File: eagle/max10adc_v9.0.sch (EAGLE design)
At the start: 206 parts, among them IC1 MAX19506, IC2 MAX19506, J1 MOLEX_BNC_73100-0105, J2 MOLEX_BNC_73100-0105, J3 MOLEX_BNC_73100-0105, J4 MOLEX_BNC_73100-0105, K1 AQY21SOP, K2 AQY21SOP, K3 AQY21SOP, K4 AQY21SOP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

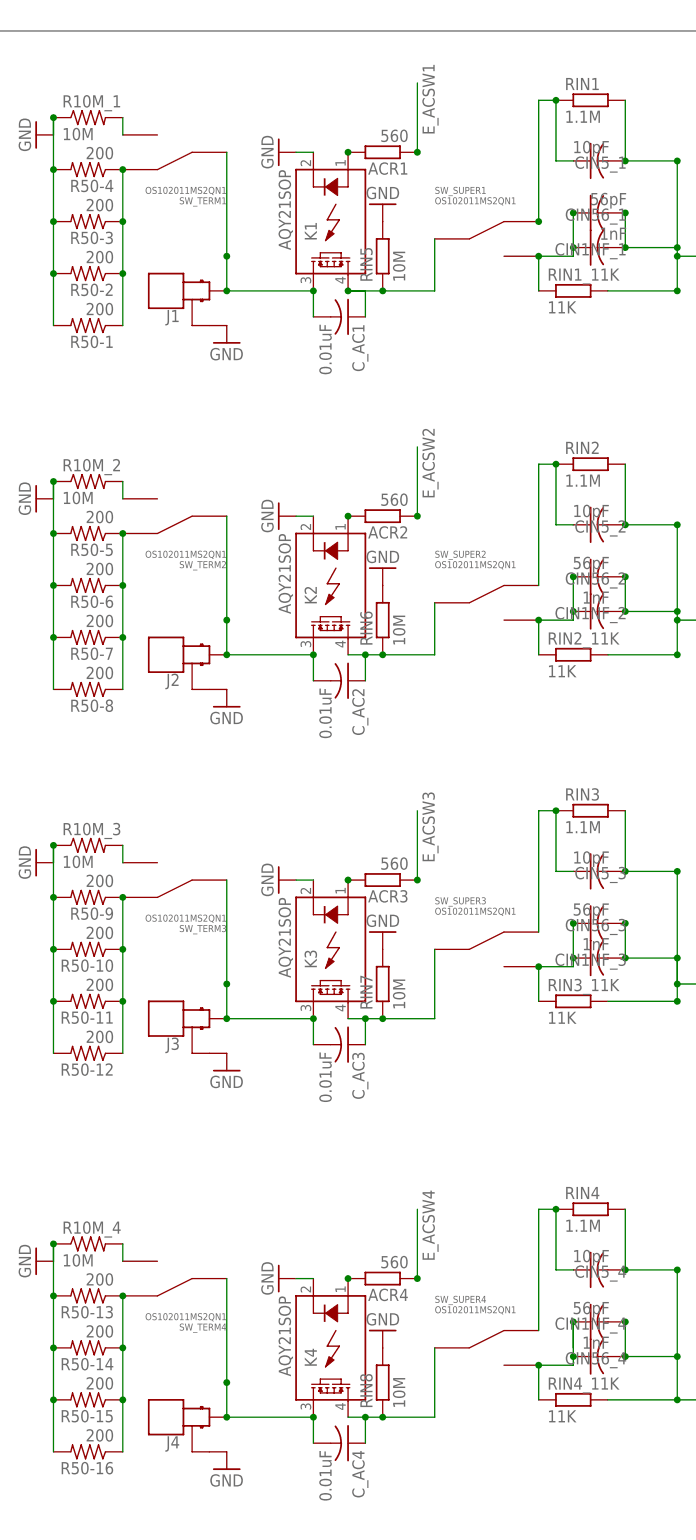
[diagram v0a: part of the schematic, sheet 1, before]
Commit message: updates for board 9.0 with dpdt switches
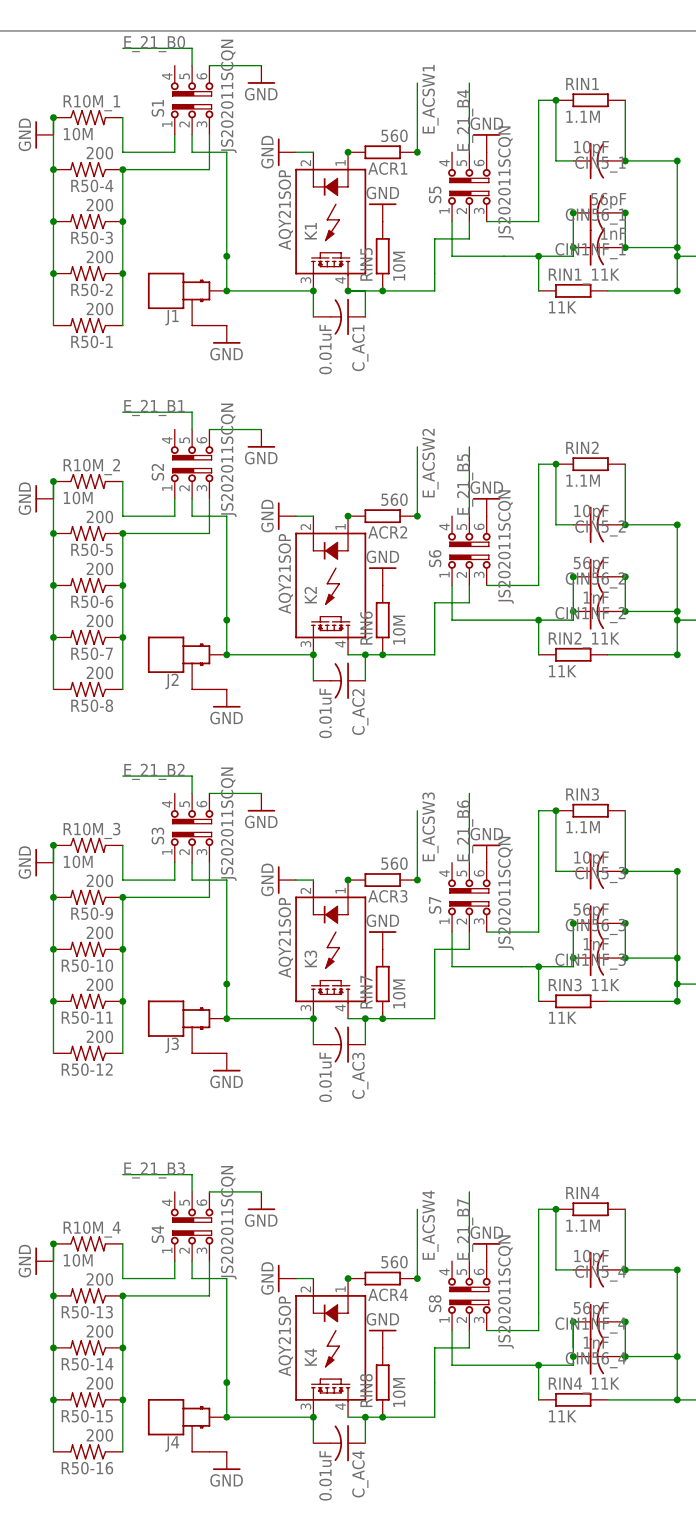
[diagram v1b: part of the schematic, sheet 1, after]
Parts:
- removed LED5, LED6, LED7, LED8: MF-LED-0805-RED, led:LEDSML0805
- removed RLED5, RLED6, RLED7, RLED8: 560, resistor:R-EU_R0805
- removed SW_5V, SW_SUPER1, SW_SUPER2, SW_SUPER3, SW_SUPER4, SW_TERM1, SW_TERM2, SW_TERM3, SW_TERM4: OS102011MS2QN1, PP_Electromechanical:SPDT_0S102011MS2QS1
- added S1, S2, S3, S4, S5, S6, S7, S8, S9: JS202011SCQN, switch-ck:JS202011SCQN
- renumbered IOEXPAND_0X24_TOP to IOEXPAND_0X21_TOP
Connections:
- removed net DCLKA1: IC1.DCLKA
- removed net DCLKA2: IC2.DCLKA
- removed net DCLKB1: IC1.DCLKB
- removed net DCLKB2: IC2.DCLKB
- removed net DORA1: IC1.DORA
- removed net DORA2: IC2.DORA
- removed net DORB1: IC1.DORB
- removed net DORB2: IC2.DORB
- removed net E_24_B0: IOEXPAND_0X21_TOP.GPB0, PIN_ANALOG_IOEXP.1
- removed net E_24_B1: IOEXPAND_0X21_TOP.GPB1, PIN_ANALOG_IOEXP.3
- removed net E_24_B2: IOEXPAND_0X21_TOP.GPB2, PIN_ANALOG_IOEXP.5
- removed net E_24_B3: IOEXPAND_0X21_TOP.GPB3, PIN_ANALOG_IOEXP.7
- removed net E_24_B4: IOEXPAND_0X21_TOP.GPB4, PIN_ANALOG_IOEXP.9
- removed net E_24_B5: IOEXPAND_0X21_TOP.GPB5, PIN_ANALOG_IOEXP.11
- removed net E_24_B6: IOEXPAND_0X21_TOP.GPB6, PIN_ANALOG_IOEXP.13
- removed net E_24_B7: IOEXPAND_0X21_TOP.GPB7, PIN_ANALOG_IOEXP.15
- removed net LED5: IOEXPAND_0X21_TOP.GPA4, LED5.A
- removed net LED6: IOEXPAND_0X21_TOP.GPA5, LED6.A
- removed net LED7: IOEXPAND_0X21_TOP.GPA6, LED7.A
- removed net LED8: IOEXPAND_0X21_TOP.GPA7, LED8.A
- removed net N$16: LED6.C, RLED6.1
- removed net N$17: LED5.C, RLED5.1
- removed net N$38: CIN1NF_2.1, CIN56_2.1, RIN2_11K.1, SW_SUPER2.2
- removed net N$40: CIN1NF_3.1, CIN56_3.1, RIN3_11K.1, SW_SUPER3.2
- removed net N$42: CIN5_3.1, RIN3.1, SW_SUPER3.1
- removed net N$52: CIN5_4.1, RIN4.1, SW_SUPER4.1
- removed net N$53: CIN1NF_4.1, CIN56_4.1, RIN4_11K.1, SW_SUPER4.2
- removed net N$61: CIN5_2.1, RIN2.1, SW_SUPER2.1
- new net E_21_B0: IOEXPAND_0X21_TOP.GPB0, S1.5
- new net E_21_B1: IOEXPAND_0X21_TOP.GPB1, S2.5
- new net E_21_B2: IOEXPAND_0X21_TOP.GPB2, S3.5
- new net E_21_B3: IOEXPAND_0X21_TOP.GPB3, S4.5
- new net E_21_B4: IOEXPAND_0X21_TOP.GPB4, S5.5
- new net E_21_B5: IOEXPAND_0X21_TOP.GPB5, S6.5
- new net E_21_B6: IOEXPAND_0X21_TOP.GPB6, S7.5
- new net E_21_B7: IOEXPAND_0X21_TOP.GPB7, S8.5
- new net E_IO_1: IOEXPAND_0X21_TOP.GPA4, PIN_ANALOG_IOEXP.1
- new net E_IO_2: IOEXPAND_0X21_TOP.GPA5, PIN_ANALOG_IOEXP.3
- new net E_IO_3: IOEXPAND_0X21_TOP.GPA6, PIN_ANALOG_IOEXP.5
- new net E_IO_4: IOEXPAND_0X21_TOP.GPA7, PIN_ANALOG_IOEXP.7
- new net N$43: CIN1NF_3.1, CIN56_3.1, RIN3_11K.1, S7.1
- new net N$51: CIN5_3.1, RIN3.1, S7.3
- new net N$56: CIN1NF_4.1, CIN56_4.1, RIN4_11K.1, S8.1
- new net N$57: CIN5_4.1, RIN4.1, S8.3
- net +3V3: now also PIN_ANALOG_IOEXP.15
- net +5V: now also S9.2; no longer SW_5V.C
- net 5VINFROMRIGHT: now also S9.3; no longer SW_5V.2
- net 5VINFROMUSB: now also S9.1; no longer SW_5V.1
- net GND: now also PIN_ANALOG_IOEXP.9, S1.6, S2.6, S3.6, S4.6, S5.6, S6.6, S7.6, S8.6; no longer RLED5.2, RLED6.2, RLED7.2, RLED8.2
- net INJ1: now also S1.2; no longer SW_TERM1.C
- net INJ2: now also S2.2; no longer SW_TERM2.C
- net INJ3: now also S3.2; no longer SW_TERM3.C
- net INJ4: now also S4.2; no longer SW_TERM4.C
- net L141_SCL: now also PIN_ANALOG_IOEXP.11
- net L21_SDA: now also PIN_ANALOG_IOEXP.13
- net N$10: now also S5.2; no longer SW_SUPER1.C
- net N$15: now also S6.2; no longer SW_SUPER2.C
- net N$19: now also CIN1NF_2.1, CIN56_2.1, RIN2_11K.1, S6.1; no longer LED7.C, RLED7.1
- net N$20: now also S5.1; no longer SW_SUPER1.2
- net N$22: now also CIN5_2.1, RIN2.1, S6.3; no longer LED8.C, RLED8.1
- net N$24: now also S1.1; no longer SW_TERM1.2
- net N$25: now also S2.3; no longer SW_TERM2.1
- net N$26: now also S3.3; no longer SW_TERM3.1
- net N$27: now also S2.1; no longer SW_TERM2.2
- net N$28: now also S4.3; no longer SW_TERM4.1
- net N$29: now also S1.3; no longer SW_TERM1.1
- net N$30: now also S3.1; no longer SW_TERM3.2
- net N$33: now also S4.1; no longer SW_TERM4.2
- net N$37: now also S5.3; no longer SW_SUPER1.1
- net N$39: now also S7.2; no longer SW_SUPER3.C
- net N$50: now also S8.2; no longer SW_SUPER4.C
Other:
- moved on the sheet: LED1, LED2, LED3, LED4, RLED1, RLED2, RLED3, RLED4

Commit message: Cleanup schematic. Fit pages to A3. Replaces some SMD resistor so all resistor symbols are the same
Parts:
- R10M_1, R10M_2, R10M_3, R10M_4, R50-1, R50-10, R50-11, R50-12, R50-13, R50-14, R50-15, R50-16, R50-2, R50-3, R50-4, R50-5, R50-6, R50-7, R50-8, R50-9, ROFFSET1, ROFFSET2, ROFFSET3, ROFFSET4: device rcl@1:R-US_R0805 -> resistor:R-EU_R0805
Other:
- note added: "3V3"
- note added: "Channel 1"
- note added: "Channel 1+2"
- note added: "Channel 2"
- note added: "Channel 3"
- note added: "Channel 3+4"
- note added: "Channel 4"
- note added: "Front-End gain and offset"
- note added: "Front-Ends"
- note added: "Misc."
- note added: "VCCA"
- note removed: "Front end gain and offset"
- note removed: "Front end oversampling switches"
- note removed: "Front ends"

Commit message: Changed values from 200 to 200R
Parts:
- R50-1, R50-10, R50-11, R50-12, R50-13, R50-14, R50-15, R50-16, R50-2, R50-3, R50-4, R50-5, R50-6, R50-7, R50-8, R50-9, ROFFSET1, ROFFSET2, ROFFSET3, ROFFSET4: value 200 -> 200R
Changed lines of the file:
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@@
 <attribute name="OC_NEWARK" value="unknown"/>
 </part>
-<part name="R50-4" library="resistor" library_urn="urn:adsk.eagle:library:348" deviceset="R-EU_" device="R0805" package3d_urn="urn:adsk.eagle:package:26059/1" value="200"/>
-<part name="R50-3" library="resistor" library_urn="urn:adsk.eagle:library:348" deviceset="R-EU_" device="R0805" package3d_urn="urn:adsk.eagle:package:26059/1" value="200"/>
-<part name="R50-2" library="resistor" library_urn="urn:adsk.eagle:library:348" deviceset="R-EU_" device="R0805" package3d_urn="urn:adsk.eagle:package:26059/1" value="200"/>
-<part name="R50-1" library="resistor" library_urn="urn:adsk.eagle:library:348" deviceset="R-EU_" device="R0805" package3d_urn="urn:adsk.eagle:package:26059/1" value="200"/>
-<part name="R50-5" library="resistor" library_urn="urn:adsk.eagle:library:348" deviceset="R-EU_" device="R0805" package3d_urn="urn:adsk.eagle:package:26059/1" value="200"/>
-<part name="R50-6" library="resistor" library_urn="urn:adsk.eagle:library:348" deviceset="R-EU_" device="R0805" package3d_urn="urn:adsk.eagle:package:26059/1" value="200"/>
-<part name="R50-7" library="resistor" library_urn="urn:adsk.eagle:library:348" deviceset="R-EU_" device="R0805" package3d_urn="urn:adsk.eagle:package:26059/1" value="200"/>
-<part name="R50-8" library="resistor" library_urn="urn:adsk.eagle:library:348" deviceset="R-EU_" device="R0805" package3d_urn="urn:adsk.eagle:package:26059/1" value="200"/>
-<part name="R50-9" library="resistor" library_urn="urn:adsk.eagle:library:348" deviceset="R-EU_" device="R0805" package3d_urn="urn:adsk.eagle:package:26059/1" value="200"/>
-<part name="R50-10" library="resistor" library_urn="urn:adsk.eagle:library:348" deviceset="R-EU_" device="R0805" package3d_urn="urn:adsk.eagle:package:26059/1" value="200"/>
-<part name="R50-11" library="resistor" library_urn="urn:adsk.eagle:library:348" deviceset="R-EU_" device="R0805" package3d_urn="urn:adsk.eagle:package:26059/1" value="200"/>
-<part name="R50-12" library="resistor" library_urn="urn:adsk.eagle:library:348" deviceset="R-EU_" device="R0805" package3d_urn="urn:adsk.eagle:package:26059/1" value="200"/>
-<part name="R50-13" library="resistor" library_urn="urn:adsk.eagle:library:348" deviceset="R-EU_" device="R0805" package3d_urn="urn:adsk.eagle:package:26059/1" value="200"/>
-<part name="R50-14" library="resistor" library_urn="urn:adsk.eagle:library:348" deviceset="R-EU_" device="R0805" package3d_urn="urn:adsk.eagle:package:26059/1" value="200"/>
-<part name="R50-15" library="resistor" library_urn="urn:adsk.eagle:library:348" deviceset="R-EU_" device="R0805" package3d_urn="urn:adsk.eagle:package:26059/1" value="200"/>
-<part name="R50-16" library="resistor" library_urn="urn:adsk.eagle:library:348" deviceset="R-EU_" device="R0805" package3d_urn="urn:adsk.eagle:package:26059/1" value="200"/>
+<part name="R50-4" library="resistor" library_urn="urn:adsk.eagle:library:348" deviceset="R-EU_" device="R0805" package3d_urn="urn:adsk.eagle:package:26059/1" value="200R"/>
+<part name="R50-3" library="resistor" library_urn="urn:adsk.eagle:library:348" deviceset="R-EU_" device="R0805" package3d_urn="urn:adsk.eagle:package:26059/1" value="200R"/>
+<part name="R50-2" library="resistor" library_urn="urn:adsk.eagle:library:348" deviceset="R-EU_" device="R0805" package3d_urn="urn:adsk.eagle:package:26059/1" value="200R"/>
+<part name="R50-1" library="resistor" library_urn="urn:adsk.eagle:library:348" deviceset="R-EU_" device="R0805" package3d_urn="urn:adsk.eagle:package:26059/1" value="200R"/>
+<part name="R50-5" library="resistor" library_urn="urn:adsk.eagle:library:348" deviceset="R-EU_" device="R0805" package3d_urn="urn:adsk.eagle:package:26059/1" value="200R"/>
+<part name="R50-6" library="resistor" library_urn="urn:adsk.eagle:library:348" deviceset="R-EU_" device="R0805" package3d_urn="urn:adsk.eagle:package:26059/1" value="200R"/>
+<part name="R50-7" library="resistor" library_urn="urn:adsk.eagle:library:348" deviceset="R-EU_" device="R0805" package3d_urn="urn:adsk.eagle:package:26059/1" value="200R"/>
+<part name="R50-8" library="resistor" library_urn="urn:adsk.eagle:library:348" deviceset="R-EU_" device="R0805" package3d_urn="urn:adsk.eagle:package:26059/1" value="200R"/>
+<part name="R50-9" library="resistor" library_urn="urn:adsk.eagle:library:348" deviceset="R-EU_" device="R0805" package3d_urn="urn:adsk.eagle:package:26059/1" value="200R"/>
+<part name="R50-10" library="resistor" library_urn="urn:adsk.eagle:library:348" deviceset="R-EU_" device="R0805" package3d_urn="urn:adsk.eagle:package:26059/1" value="200R"/>
+<part name="R50-11" library="resistor" library_urn="urn:adsk.eagle:library:348" deviceset="R-EU_" device="R0805" package3d_urn="urn:adsk.eagle:package:26059/1" value="200R"/>
+<part name="R50-12" library="resistor" library_urn="urn:adsk.eagle:library:348" deviceset="R-EU_" device="R0805" package3d_urn="urn:adsk.eagle:package:26059/1" value="200R"/>
+<part name="R50-13" library="resistor" library_urn="urn:adsk.eagle:library:348" deviceset="R-EU_" device="R0805" package3d_urn="urn:adsk.eagle:package:26059/1" value="200R"/>
+<part name="R50-14" library="resistor" library_urn="urn:adsk.eagle:library:348" deviceset="R-EU_" device="R0805" package3d_urn="urn:adsk.eagle:package:26059/1" value="200R"/>
+<part name="R50-15" library="resistor" library_urn="urn:adsk.eagle:library:348" deviceset="R-EU_" device="R0805" package3d_urn="urn:adsk.eagle:package:26059/1" value="200R"/>
+<part name="R50-16" library="resistor" library_urn="urn:adsk.eagle:library:348" deviceset="R-EU_" device="R0805" package3d_urn="urn:adsk.eagle:package:26059/1" value="200R"/>
 <part name="U340G" library="usb-serial" deviceset="CH340G" device=""/>
 <part name="Y1" library="SparkFun-FreqCtrl" deviceset="CRYSTAL" device="HC49US" value="ABL-12.000MHZ-B2"/>
@@
 <attribute name="MPN" value="MF-CAP-0805-1uF"/>
 </part>
-<part name="ROFFSET1" library="resistor" library_urn="urn:adsk.eagle:library:348" deviceset="R-EU_" device="R0805" package3d_urn="urn:adsk.eagle:package:26059/1" value="200"/>
-<part name="ROFFSET2" library="resistor" library_urn="urn:adsk.eagle:library:348" deviceset="R-EU_" device="R0805" package3d_urn="urn:adsk.eagle:package:26059/1" value="200"/>
-<part name="ROFFSET3" library="resistor" library_urn="urn:adsk.eagle:library:348" deviceset="R-EU_" device="R0805" package3d_urn="urn:adsk.eagle:package:26059/1" value="200"/>
-<part name="ROFFSET4" library="resistor" library_urn="urn:adsk.eagle:library:348" deviceset="R-EU_" device="R0805" package3d_urn="urn:adsk.eagle:package:26059/1" value="200"/>
+<part name="ROFFSET1" library="resistor" library_urn="urn:adsk.eagle:library:348" deviceset="R-EU_" device="R0805" package3d_urn="urn:adsk.eagle:package:26059/1" value="200R"/>
+<part name="ROFFSET2" library="resistor" library_urn="urn:adsk.eagle:library:348" deviceset="R-EU_" device="R0805" package3d_urn="urn:adsk.eagle:package:26059/1" value="200R"/>
+<part name="ROFFSET3" library="resistor" library_urn="urn:adsk.eagle:library:348" deviceset="R-EU_" device="R0805" package3d_urn="urn:adsk.eagle:package:26059/1" value="200R"/>
+<part name="ROFFSET4" library="resistor" library_urn="urn:adsk.eagle:library:348" deviceset="R-EU_" device="R0805" package3d_urn="urn:adsk.eagle:package:26059/1" value="200R"/>
 <part name="U$1" library="SparkFun-PowerSymbols" library_urn="urn:adsk.eagle:library:530" deviceset="VCCA" device=""/>
 <part name="U$2" library="SparkFun-PowerSymbols" library_urn="urn:adsk.eagle:library:530" deviceset="VCCA" device=""/>
